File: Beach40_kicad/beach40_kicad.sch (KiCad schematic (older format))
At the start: 83 parts, among them K1 RELAY_2RT, P1 LO In, P2 Mic In, P3 Audio Out, P4 ANT, Q1 BC548, Q2 2N2222, Q3 BD139, Q4 BD139, Q5 BC548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

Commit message: more tweaks to schematic, another attempt at layout starting, missing footprints though
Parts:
- removed C11: 4.7n, Capacitors_ThroughHole:Capacitor3MMDiscRM2.5, symbol CAP
- removed C30: 47u, Capacitors_ThroughHole:Capacitor3MMDiscRM2.5, symbol C_POL
- added C11: 47u, symbol C_POL
- added C30: 100n, symbol CAP
- C13: value 100n -> 4.7n; footprint Capacitors_ThroughHole:Capacitor3MMDiscRM2.5 -> (none)
- R2: value R -> 330
- R20: value 22 -> 2.2; footprint FT:RES_AXIAL_400MIL -> (none)
- R7: value 22 -> 18; footprint FT:RES_AXIAL_400MIL -> (none)
- R8: value 2.2 -> 2.2k; footprint FT:RES_AXIAL_400MIL -> (none)
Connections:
- net GND: now also R7.2, C30.2; no longer C13.2, R20.2
- net at U1.1 (Gain): now also R8.2, C11.1 (+)
- net at C12.1 (+), U1.5: now also C13.1, R20.1; no longer R7.1, R8.1
- new net: C11.2 (-), R7.1
- new net: C13.2, R8.1
- new net: C30.1, R20.2
- no-connect marks 0 -> 3
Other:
- moved on the sheet: C12, P3

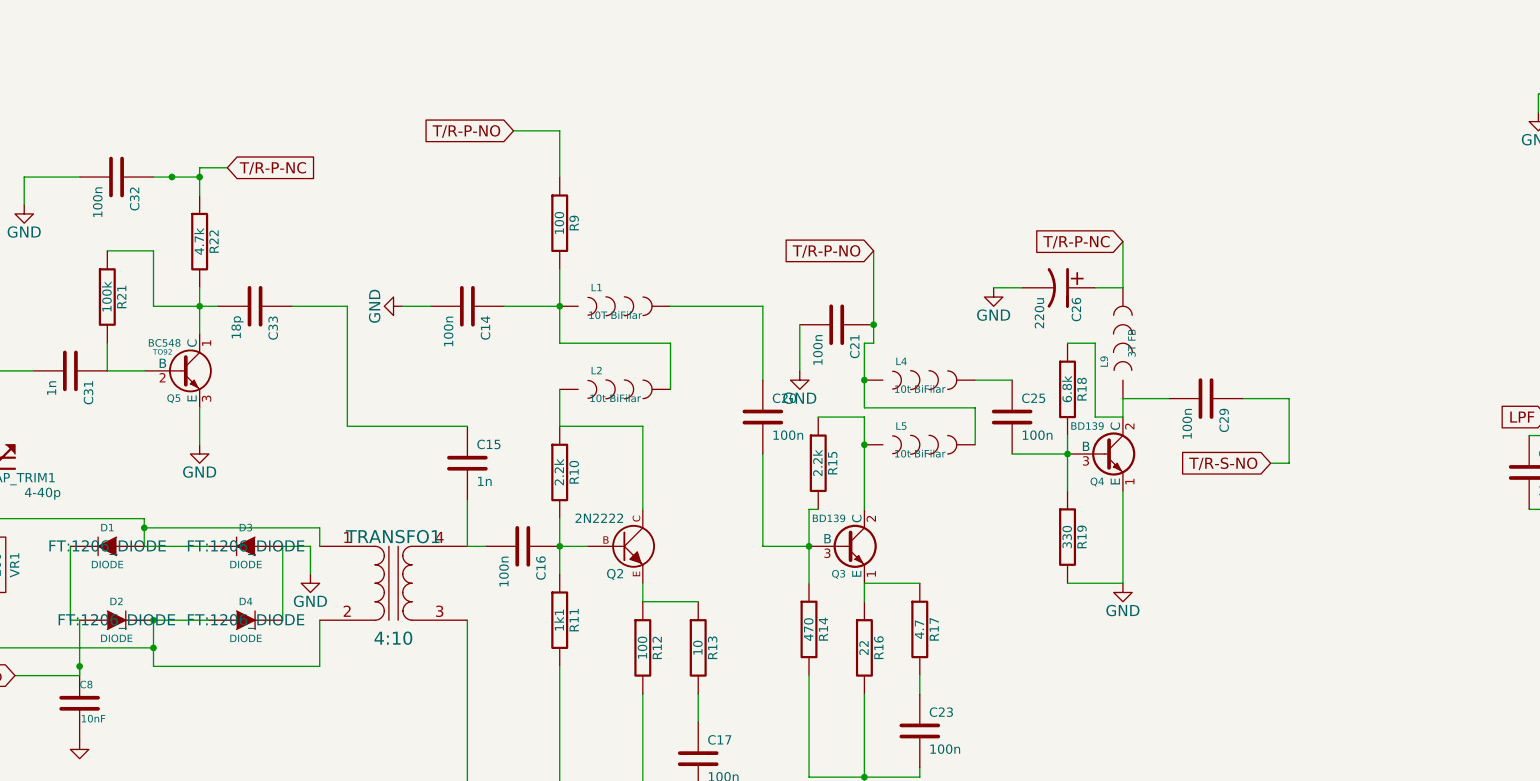
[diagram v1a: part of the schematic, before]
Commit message: custom chokes added for the 10 turn bifilar chokes. still some issues, libraries are a bit skeewiff
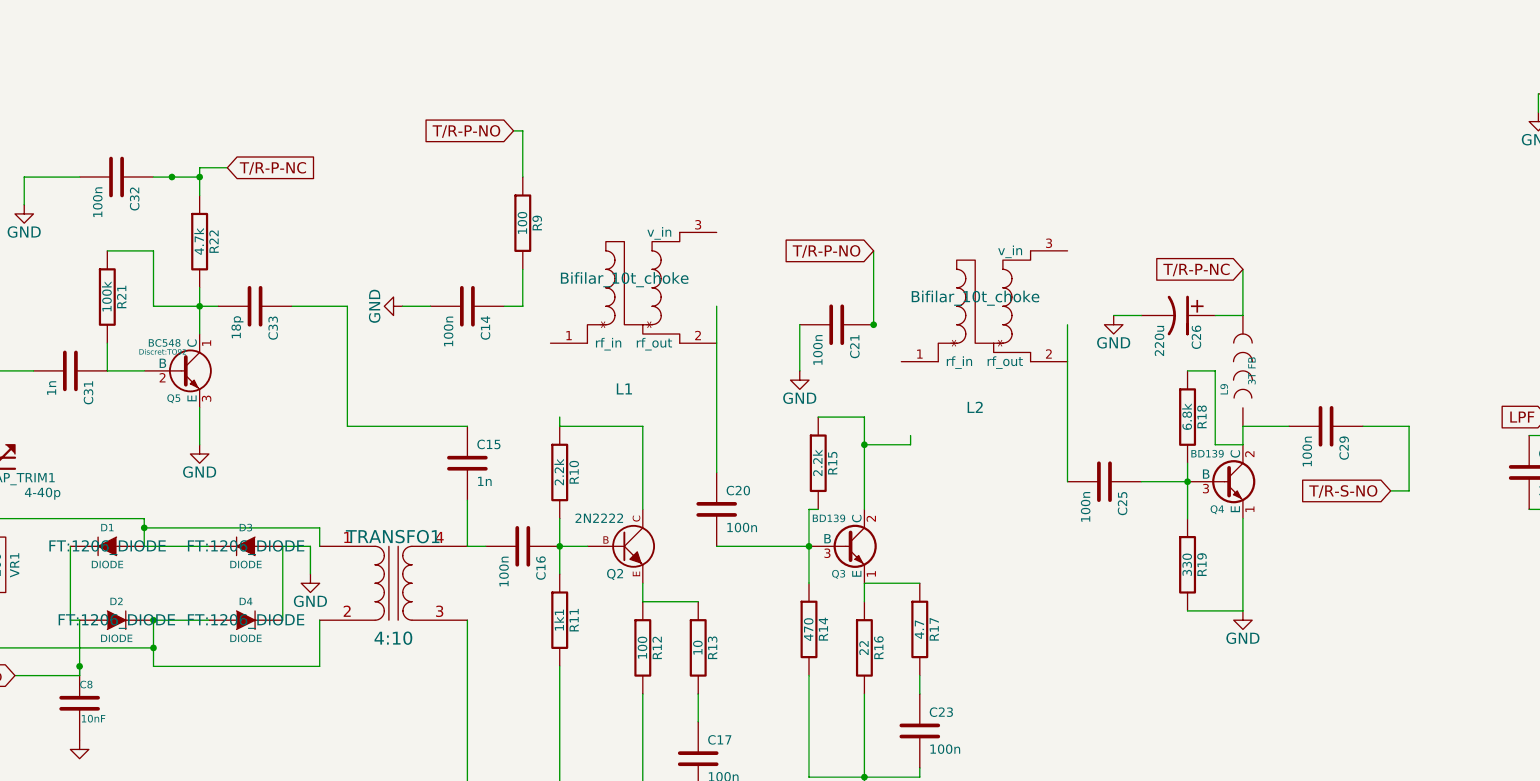
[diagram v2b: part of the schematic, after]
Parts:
- removed L1: 10T BiFilar, FT:IND_SRP1040, symbol INDUCTOR
- removed L2, L4, L5: 10t BiFilar, FT:IND_SRP1040, symbol INDUCTOR
- added L1, L2: Bifilar_10t_choke, custom_chokes:Biflar_10t_choke, symbol Bifilar_10t_choke
- C11, C13, C30, C31, C32, C33: footprint (none) -> Capacitors_ThroughHole:Capacitor3MMDiscRM2.5
- Q5: footprint TO92 -> Discret:TO92
- R20, R7, R8: footprint (none) -> FT:RES_AXIAL_400MIL
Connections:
- net at C25.1: now also Q4.3 (B), R18.2, R19.1
- now unconnected: C25.2
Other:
- moved on the sheet: C20, C25, C26, C29, L9, Q4, R18, R19, R9

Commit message: reverted a bit, back to SMD components, much more better! Actual start of layout now.
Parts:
- removed P2: Mic In, symbol CON_JACK_MONO_SW
- removed P3: Audio Out, symbol CON_JACK_MONO_SW
- removed TRANSFO1: 4:10, symbol TRANSFORMER
- added P2: MIC_IN, symbol CONN_01X02
- added P3: Audio Out, symbol CONN_01X02
- added T1: 4:10_Transformer, symbol 4:10_Transformer
- C1, C13, C14, C15, C16, C17, C18, C19, C2, C20, C21, C22, C23, C24, C25, C27, C28, C29, C3, C30, C31, C32, C33, C4: footprint Capacitors_ThroughHole:Capacitor3MMDiscRM2.5 -> FT:1210_CAP
- C11: footprint Capacitors_ThroughHole:Capacitor3MMDiscRM2.5 -> FT:CAP_ELECTRO_D4S1.8
- C8: footprint Capacitors_ThroughHole:Capacitor3MMDiscRM2.5 -> FT:0603_CAP
- CAP_TRIM1: footprint (none) -> Discret:C2
- L3, L6, L7, L8: footprint Choke_Axial_ThroughHole:Choke_Horizontal_RM15mm -> FT:1206
- PTT1: footprint (none) -> Pin_Headers:Pin_Header_Straight_1x02
- Q1: footprint Housings_TO-92:TO-92-Bipolar-inline-wide-BCE -> Housings_TO-92:TO-92_Inline_Narrow_Oval
- Q2: footprint Housings_TO-92:TO-92-Bipolar-inline-wide-BCE -> FT:SOT23_TRANSISTOR
- Q3, Q4: footprint Transistors_TO-220:TO-220_Bipolar-BCE_Vertical_LargePads -> Discret:TO220_VERT
- Q5: footprint Discret:TO92 -> Housings_TO-92:TO-92_Inline_Narrow_Oval
- R1, R10, R11, R12, R13, R14, R15, R16, R17, R18, R19, R2, R20, R3, R4, R5, R6, R7, R8, R9: footprint FT:RES_AXIAL_400MIL -> FT:1210
- R21, R22: footprint (none) -> FT:1210
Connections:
- wire segments 165 -> 170
- no-connect marks 3 -> 1

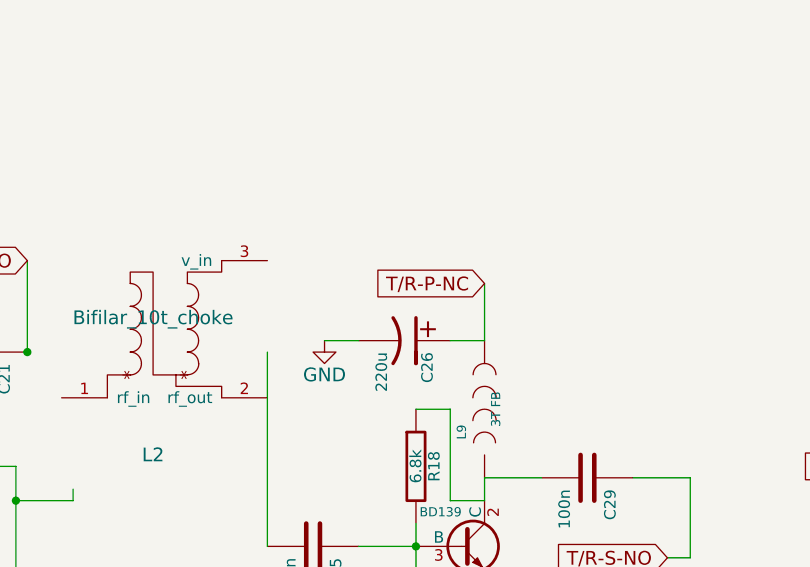
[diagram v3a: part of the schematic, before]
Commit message: - a mistake or two in the schematic! - just noticed the relay is not correct, pin mappings wierd, custom part time! - more layout
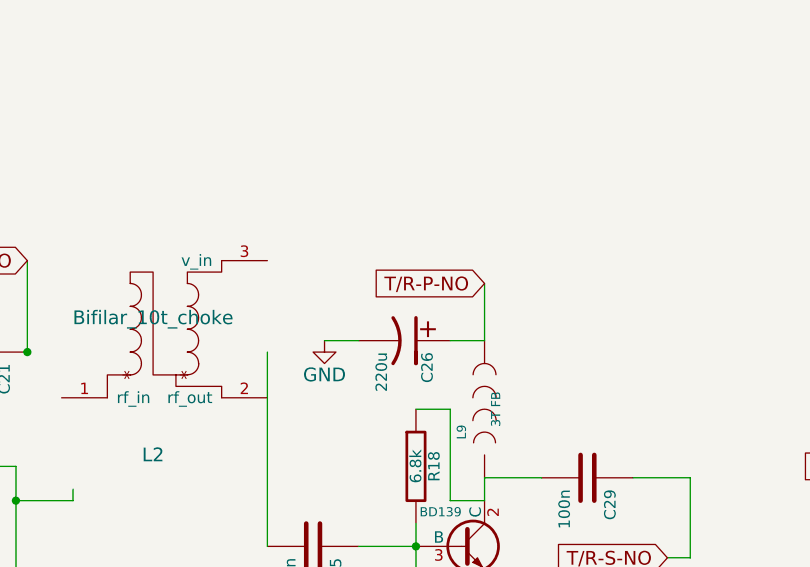
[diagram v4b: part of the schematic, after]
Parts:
- C8: footprint FT:0603_CAP -> FT:1210_CAP
- K1: footprint Relays_ThroughHole:Relais_DPDT_Schrack-RT2_RM5mm -> Relays_ThroughHole:Relay_DPDT_Schrack-RT2_RM5mm
- P2, P3: footprint (none) -> Pin_Headers:Pin_Header_Straight_1x02
- T1: footprint (none) -> custom_chokes:4_10_Transformer
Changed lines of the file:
@@
 F 0 "C8" H 3250 5850 40  0000 L CNN
 F 1 "10nF" H 3256 5665 40  0000 L CNN
-F 2 "FT:0603_CAP" H 3288 5600 30  0001 C CNN
+F 2 "FT:1210_CAP" H 3288 5600 30  0001 C CNN
 F 3 "" H 3250 5750 60  0000 C CNN
 	1    3250 5750
@@
 F 0 "K1" H 12200 2350 50  0000 C CNN
 F 1 "RELAY_2RT" H 12400 1450 50  0000 C CNN
-F 2 "Relays_ThroughHole:Relais_DPDT_Schrack-RT2_RM5mm" H 12250 1950 60  0001 C CNN
+F 2 "Relays_ThroughHole:Relay_DPDT_Schrack-RT2_RM5mm" H 12250 1950 60  0001 C CNN
 F 3 "" H 12250 1950 60  0000 C CNN
 	1    12250 1950
@@
 T/R-P-NO
 Text GLabel 9550 3400 0    60   Input ~ 0
-T/R-P-NC
+T/R-P-NO
 $Comp
 L INDUCTOR L3
@@
 F 0 "P3" H 8950 8750 50  0000 C CNN
 F 1 "Audio Out" V 9050 8600 50  0000 C CNN
-F 2 "" H 8950 8600 60  0001 C CNN
+F 2 "Pin_Headers:Pin_Header_Straight_1x02" H 8950 8600 60  0001 C CNN
 F 3 "" H 8950 8600 60  0000 C CNN
 	1    8950 8600
@@
 F 0 "P2" H 2300 9650 50  0000 C CNN
 F 1 "MIC_IN" V 2400 9500 50  0000 C CNN
-F 2 "" H 2300 9500 60  0001 C CNN
+F 2 "Pin_Headers:Pin_Header_Straight_1x02" H 2300 9500 60  0001 C CNN
 F 3 "" H 2300 9500 60  0000 C CNN
 	1    2300 9500
@@
 F 0 "T1" H 4950 5000 60  0000 C CNN
 F 1 "4:10_Transformer" H 4950 5450 60  0000 C CNN
-F 2 "" H 4950 5150 60  0001 C CNN
+F 2 "custom_chokes:4_10_Transformer" H 4950 5150 60  0001 C CNN
 F 3 "" H 4950 5150 60  0000 C CNN
 	1    4950 5150

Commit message: new relay footprint that matches the schematic some more layout, RF path not good though.
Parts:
- K1: footprint Relays_ThroughHole:Relay_DPDT_Schrack-RT2_RM5mm -> custom_relay:Relay_DPDT_Custom
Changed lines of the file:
@@
 F 0 "K1" H 12200 2350 50  0000 C CNN
 F 1 "RELAY_2RT" H 12400 1450 50  0000 C CNN
-F 2 "Relays_ThroughHole:Relay_DPDT_Schrack-RT2_RM5mm" H 12250 1950 60  0001 C CNN
+F 2 "custom_relay:Relay_DPDT_Custom" H 12250 1950 60  0001 C CNN
 F 3 "" H 12250 1950 60  0000 C CNN
 	1    12250 1950

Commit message: more mucking about!
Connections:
- wire segments 170 -> 176
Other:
- moved on the sheet: C14, C21, R9
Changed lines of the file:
@@
 L R R9
 U 1 1 54CC9050
-P 5650 3150
-F 0 "R9" V 5730 3150 50  0000 C CNN
-F 1 "100" V 5650 3150 50  0000 C CNN
-F 2 "FT:1210" H 5650 3150 60  0001 C CNN
-F 3 "" H 5650 3150 60  0000 C CNN
-	1    5650 3150
+P 6650 2400
+F 0 "R9" V 6730 2400 50  0000 C CNN
+F 1 "100" V 6650 2400 50  0000 C CNN
+F 2 "FT:1210" H 6650 2400 60  0001 C CNN
+F 3 "" H 6650 2400 60  0000 C CNN
+	1    6650 2400
 	1    0    0    -1
 $EndComp
@@
 L CAP C14
 U 1 1 54CC91CC
-P 5350 3600
-F 0 "C14" H 5400 3700 50  0000 L CNN
-F 1 "100n" H 5400 3500 50  0000 L CNN
-F 2 "FT:1210_CAP" H 5350 3600 60  0001 C CNN
-F 3 "" H 5350 3600 60  0000 C CNN
-	1    5350 3600
+P 6350 2850
+F 0 "C14" H 6400 2950 50  0000 L CNN
+F 1 "100n" H 6400 2750 50  0000 L CNN
+F 2 "FT:1210_CAP" H 6350 2850 60  0001 C CNN
+F 3 "" H 6350 2850 60  0000 C CNN
+	1    6350 2850
 	0    1    1    0
 $EndComp
@@
 L CAP C21
 U 1 1 54CCABCB
-P 7350 3700
-F 0 "C21" H 7400 3800 50  0000 L CNN
-F 1 "100n" H 7400 3600 50  0000 L CNN
-F 2 "FT:1210_CAP" H 7350 3700 60  0001 C CNN
-F 3 "" H 7350 3700 60  0000 C CNN
-	1    7350 3700
-	0    1    1    0
-$EndComp
-Connection ~ 7550 3700
+P 8350 2750
+F 0 "C21" H 8400 2850 50  0000 L CNN
+F 1 "100n" H 8400 2650 50  0000 L CNN
+F 2 "FT:1210_CAP" H 8350 2750 60  0001 C CNN
+F 3 "" H 8350 2750 60  0000 C CNN
+	1    8350 2750
+	0    1    1    0
+$EndComp
+Connection ~ 8550 2750
 Wire Wire Line
 	5350 5200 5350 6250
@@
 L GND #PWR03
 U 1 1 54CCEC68
-P 7150 3950
-F 0 "#PWR03" H 7150 3700 60  0001 C CNN
-F 1 "GND" H 7150 3800 60  0000 C CNN
-F 2 "" H 7150 3950 60  0001 C CNN
-F 3 "" H 7150 3950 60  0000 C CNN
-	1    7150 3950
-	1    0    0    -1
-$EndComp
-Wire Wire Line
-	7150 3700 7150 3950
+P 8150 3000
+F 0 "#PWR03" H 8150 2750 60  0001 C CNN
+F 1 "GND" H 8150 2850 60  0000 C CNN
+F 2 "" H 8150 3000 60  0001 C CNN
+F 3 "" H 8150 3000 60  0000 C CNN
+	1    8150 3000
+	1    0    0    -1
+$EndComp
+Wire Wire Line
+	8150 2750 8150 3000
 $Comp
 L CAP C15
@@
 Wire Wire Line
 	12650 1950 13050 1950
-Text GLabel 7550 3300 0    60   Input ~ 0
+Text GLabel 8550 2350 0    60   Input ~ 0
 T/R-P-NO
 Text GLabel 9550 3400 0    60   Input ~ 0
@@
 Wire Wire Line
 	2100 7550 2100 7400
-Text GLabel 5600 2650 0    60   Input ~ 0
+Text GLabel 6600 1900 0    60   Input ~ 0
 T/R-P-NO
 Wire Wire Line
@@
 L GND #PWR020
 U 1 1 54FA04E1
-P 5000 3600
-F 0 "#PWR020" H 5000 3350 60  0001 C CNN
-F 1 "GND" H 5000 3450 60  0000 C CNN
-F 2 "" H 5000 3600 60  0001 C CNN
-F 3 "" H 5000 3600 60  0000 C CNN
-	1    5000 3600
-	0    1    1    0
-$EndComp
-Wire Wire Line
-	5150 3600 5000 3600
+P 6000 2850
+F 0 "#PWR020" H 6000 2600 60  0001 C CNN
+F 1 "GND" H 6000 2700 60  0000 C CNN
+F 2 "" H 6000 2850 60  0001 C CNN
+F 3 "" H 6000 2850 60  0000 C CNN
+	1    6000 2850
+	0    1    1    0
+$EndComp
+Wire Wire Line
+	6150 2850 6000 2850
 Wire Wire Line
 	11250 1700 11250 2200
@@
 $EndComp
 Wire Wire Line
-	7500 4350 7750 4350
-Wire Wire Line
-	7750 4350 7750 4300
-Wire Wire Line
-	8600 3700 8600 4550
-Wire Wire Line
 	9000 4550 9250 4550
 $Comp
@@
 $EndComp
 Wire Wire Line
-	5550 3600 5650 3600
-Wire Wire Line
-	5850 4200 5850 4250
-Wire Wire Line
-	6700 3600 6700 4500
-Wire Wire Line
-	5650 3600 5650 3400
-Wire Wire Line
-	5600 2650 5650 2650
-Wire Wire Line
-	5650 2650 5650 2900
-Wire Wire Line
-	7550 3300 7550 3700
+	6550 2850 6650 2850
+Wire Wire Line
+	6650 2850 6650 2650
+Wire Wire Line
+	6600 1900 6650 1900
+Wire Wire Line
+	6650 1900 6650 2150
+Wire Wire Line
+	8550 2350 8550 2750
 $Comp
 L GND #PWR025
@@
 Wire Wire Line
 	5250 5200 5350 5200
+Wire Wire Line
+	5800 3800 5800 4050
+Wire Wire Line
+	5800 4050 6000 4050
+Wire Wire Line
+	6000 4050 6000 4250
+Connection ~ 6000 4250
+Wire Wire Line
+	6700 3800 6700 4500
+Wire Wire Line
+	6700 3200 6700 2750
+Wire Wire Line
+	6700 2750 6650 2750
+Connection ~ 6650 2750
+Wire Wire Line
+	7500 4350 7700 4350
+Wire Wire Line
+	7700 4350 7700 3900
+Wire Wire Line
+	8600 3300 8600 2750
+Wire Wire Line
+	8600 2750 8550 2750
+Wire Wire Line
+	8600 3900 8600 4550
 $EndSCHEMATC
